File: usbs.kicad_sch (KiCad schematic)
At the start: 34 parts, among them J2 USB-A_Amphenol_UE27AC54100, J3 USB-C_GCT_USB4105-GF-A, J4 USB-C_GCT_USB4105-GF-A, U3 FT4232H_VQFN, Y1 Resonator_12MHz_ABM8G

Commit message: [#93514] Add separating lines, clean schematics
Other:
- moved on the sheet: D6, J3, R30, R31

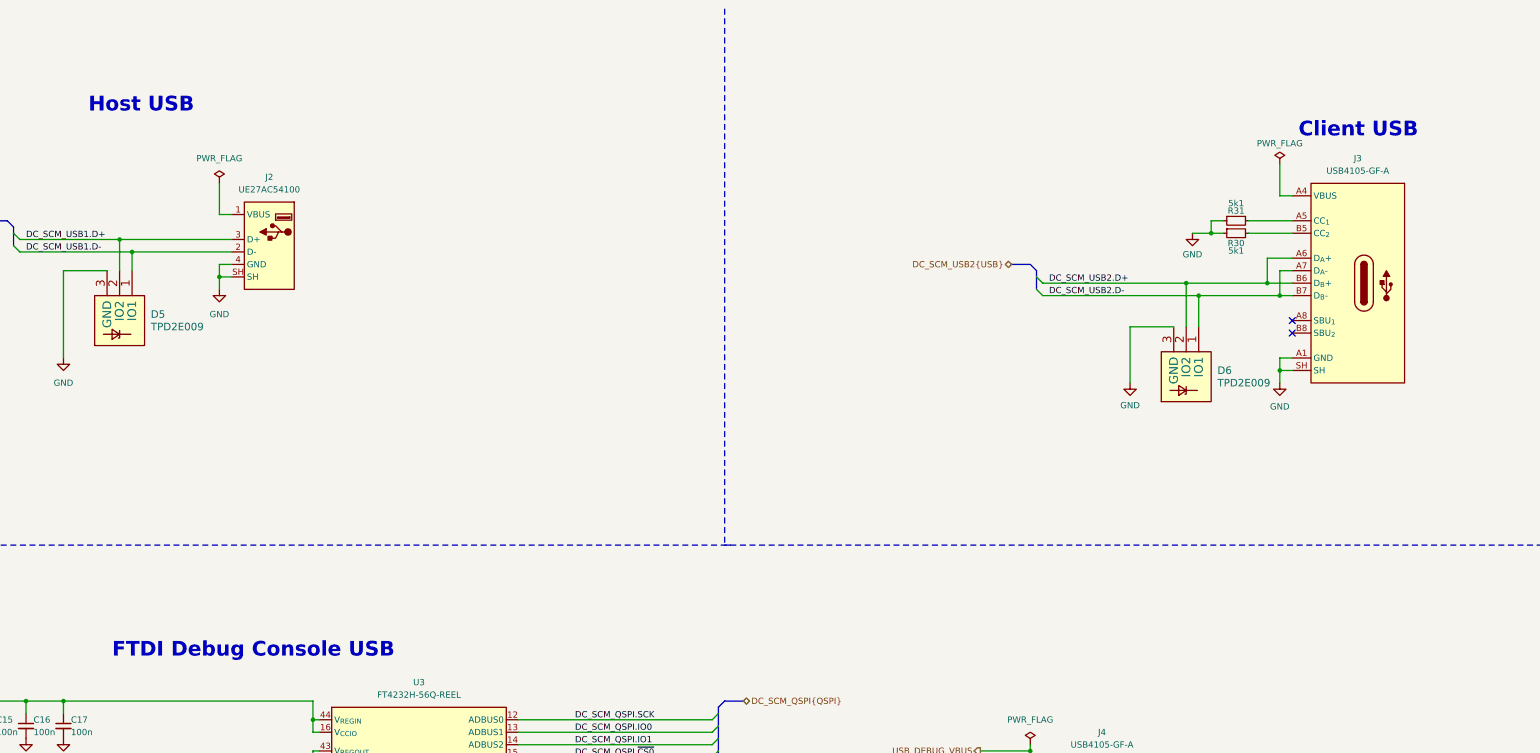
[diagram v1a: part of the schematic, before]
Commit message: [#93514] Align items to grid, add NC-SI testpads
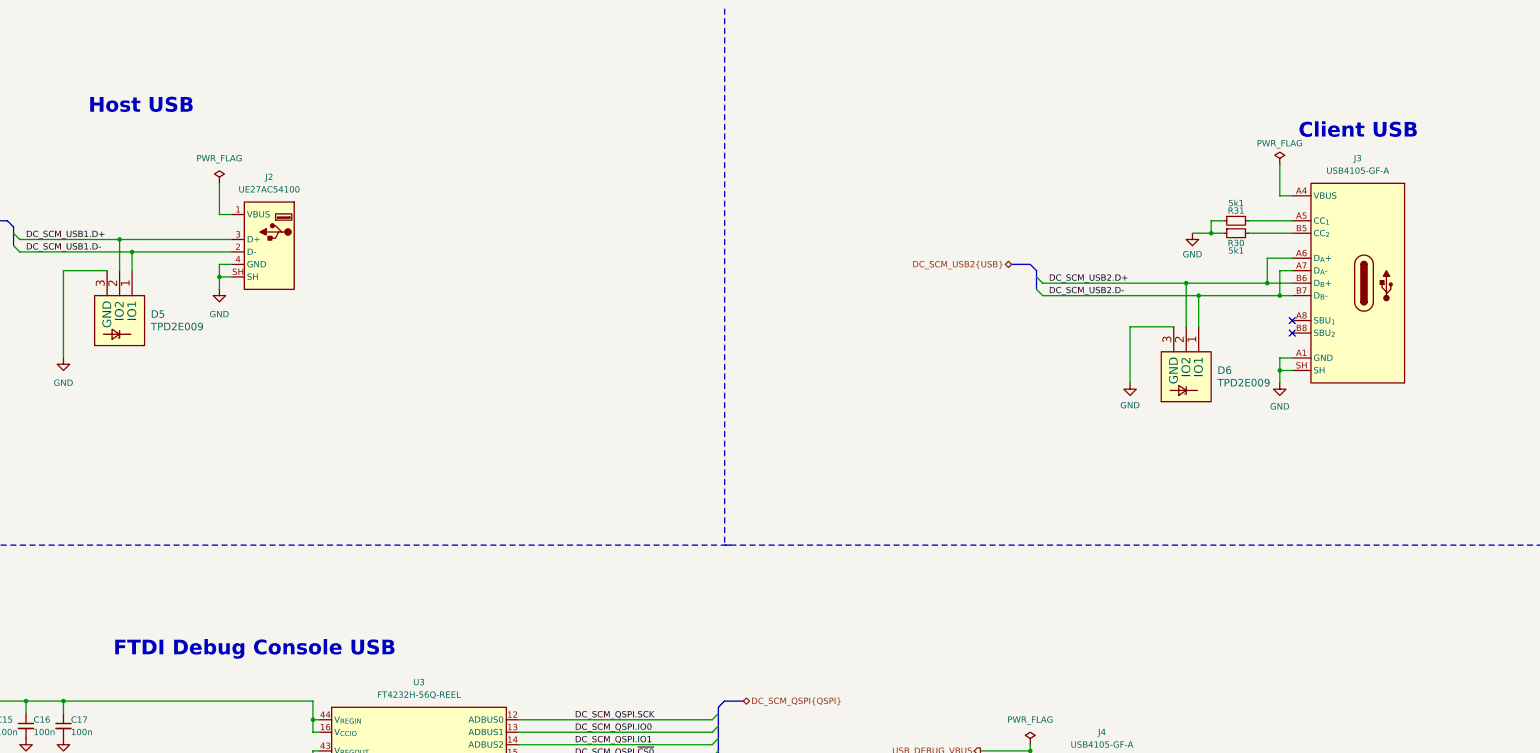
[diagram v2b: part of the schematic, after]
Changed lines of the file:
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@@
 	(text "FTDI Debug Console USB"
 		(exclude_from_sim no)
-		(at 82.296 145.034 0)
+		(at 82.55 144.78 0)
 		(effects
 			(font
@@
 	(text "Host USB"
 		(exclude_from_sim no)
-		(at 77.47 34.036 0)
+		(at 77.47 34.29 0)
 		(effects
 			(font
@@
 	(text "Client USB"
 		(exclude_from_sim no)
-		(at 323.85 39.116 0)
+		(at 323.85 39.37 0)
 		(effects
 			(font

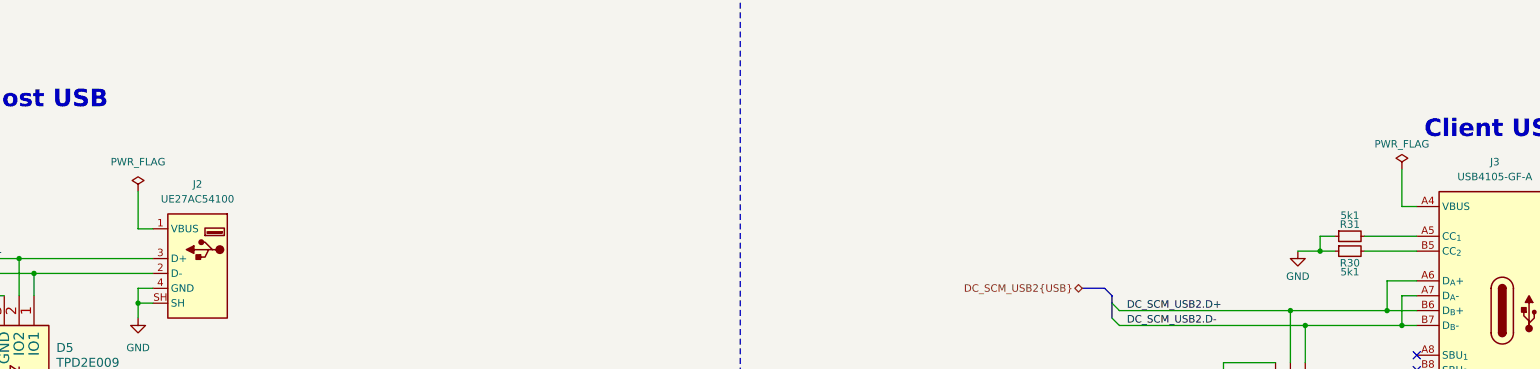
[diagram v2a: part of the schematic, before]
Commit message: [#93514] Add no connect to Host/Client USB VBUS
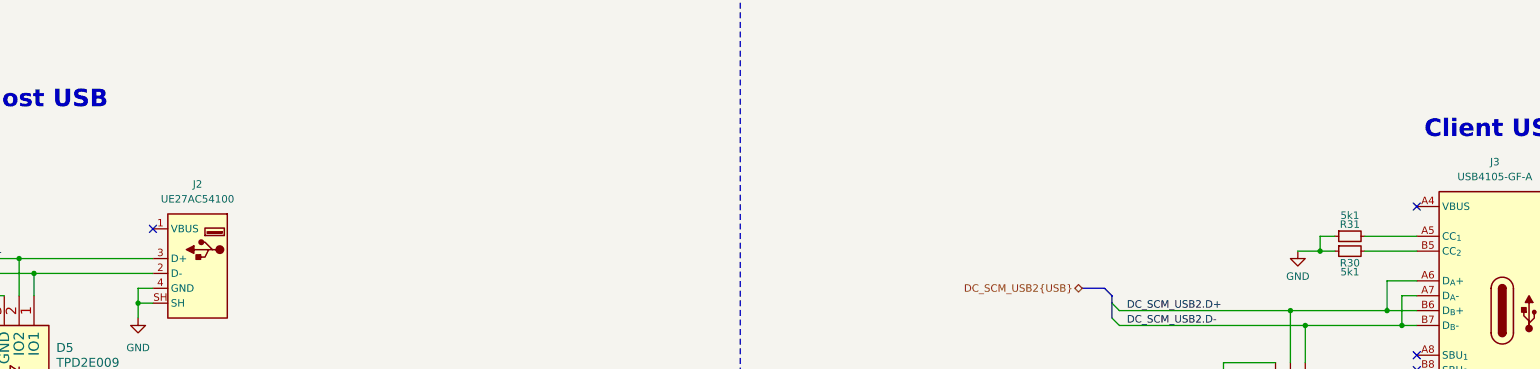
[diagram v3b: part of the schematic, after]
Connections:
- no-connect marks 32 -> 34
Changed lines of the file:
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@@
 	)
 	(no_connect
+		(at 322.58 50.8)
+	)
+	(no_connect
+		(at 106.68 54.61)
+	)
+	(no_connect
 		(at 165.1 175.26)
 	)
@@
 	(wire
 		(pts
-			(xy 320.04 50.8) (xy 322.58 50.8)
-		)
-		(stroke
-			(width 0)
-			(type default)
-		)
-	)
-	(wire
-		(pts
 			(xy 265.43 185.42) (xy 270.51 185.42)
 		)
@@
 	(wire
 		(pts
-			(xy 104.14 48.26) (xy 104.14 54.61)
-		)
-		(stroke
-			(width 0)
-			(type default)
-		)
-	)
-	(wire
-		(pts
 			(xy 267.97 205.74) (xy 267.97 203.2)
 		)
@@
 	(wire
 		(pts
-			(xy 320.04 44.45) (xy 320.04 50.8)
-		)
-		(stroke
-			(width 0)
-			(type default)
-		)
-	)
-	(wire
-		(pts
 			(xy 83.82 59.69) (xy 106.68 59.69)
 		)
@@
 		)
 	)
-	(wire
-		(pts
-			(xy 104.14 54.61) (xy 106.68 54.61)
-		)
-		(stroke
-			(width 0)
-			(type default)
-		)
-	)
 	(label "XO"
 		(at 115.57 217.17 0)
@@
 	)
 	(symbol
-		(lib_id "antmicropower:PWR_FLAG")
-		(at 104.14 48.26 0)
-		(unit 1)
-		(exclude_from_sim no)
-		(in_bom yes)
-		(on_board yes)
-		(dnp no)
-		(fields_autoplaced yes)
-		(property "Reference" "#FLG06"
-			(at 104.14 46.355 0)
-			(effects
-				(font
-					(size 1.27 1.27)
-				)
-				(hide yes)
-			)
-		)
-		(property "Value" "PWR_FLAG"
-			(at 104.14 43.18 0)
-			(effects
-				(font
-					(size 1.27 1.27)
-				)
-			)
-		)
-		(property "Footprint" ""
-			(at 104.14 48.26 0)
-			(effects
-				(font
-					(size 1.27 1.27)
-				)
-				(hide yes)
-			)
-		)
-		(property "Datasheet" ""
-			(at 104.14 48.26 0)
-			(effects
-				(font
-					(size 1.27 1.27)
-				)
-				(hide yes)
-			)
-		)
-		(property "Description" ""
-			(at 104.14 50.8 0)
-			(effects
-				(font
-					(size 1.27 1.27)
-				)
-				(justify left bottom)
-				(hide yes)
-			)
-		)
-		(pin "1"
-		)
-		(instances
-			(project "bmc-breakout-board"
-				(path "/5d67ef28-5805-4f87-b722-2926dabf7f6e/07ab1158-ddfb-42f0-9fa7-f1beb51ab908"
-					(reference "#FLG06")
-					(unit 1)
-				)
-			)
-		)
-	)
-	(symbol
 		(lib_name "FB_600Z_0.5A_Murata-BLM18AG_0603_1")
 		(lib_id "antmicroFerriteBeadsandChips:FB_600Z_0.5A_Murata-BLM18AG_0603")
@@
 					(unit 1)
 				)
-			)
-		)
-	)
-	(symbol
-		(lib_id "antmicropower:PWR_FLAG")
-		(at 320.04 44.45 0)
-		(unit 1)
-		(exclude_from_sim no)
-		(in_bom yes)
-		(on_board yes)
-		(dnp no)
-		(property "Reference" "#FLG07"
-			(at 320.04 42.545 0)
-			(effects
-				(font
-					(size 1.27 1.27)
-				)
-				(hide yes)
-			)
-		)
-		(property "Value" "PWR_FLAG"
-			(at 320.04 40.132 0)
-			(effects
-				(font
-					(size 1.27 1.27)
-				)
-			)
-		)
-		(property "Footprint" ""
-			(at 320.04 44.45 0)
-			(effects
-				(font
-					(size 1.27 1.27)
-				)
-				(hide yes)
-			)
-		)
-		(property "Datasheet" ""
-			(at 320.04 44.45 0)
-			(effects
-				(font
-					(size 1.27 1.27)
-				)
-				(hide yes)
-			)
-		)
-		(property "Description" ""
-			(at 320.04 46.99 0)
-			(effects
-				(font
-					(size 1.27 1.27)
-				)
-				(justify left bottom)
-				(hide yes)
-			)
-		)
-		(pin "1"
-		)
-		(instances
-			(project "bmc-breakout-board"
-				(path "/5d67ef28-5805-4f87-b722-2926dabf7f6e/07ab1158-ddfb-42f0-9fa7-f1beb51ab908"
-					(reference "#FLG07")
-					(unit 1)
-				)

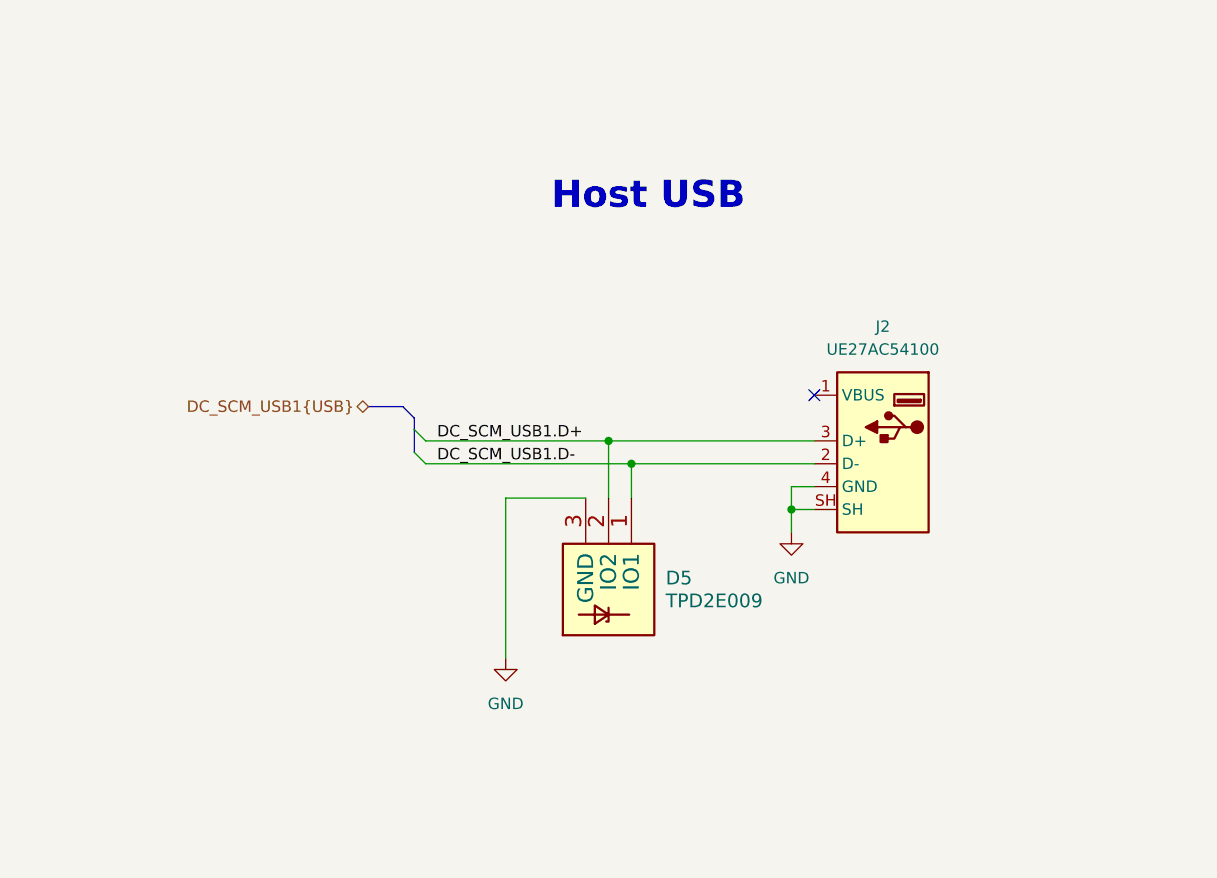
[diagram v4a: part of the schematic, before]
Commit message: [#93949] change USB HOST from USB A to USB C
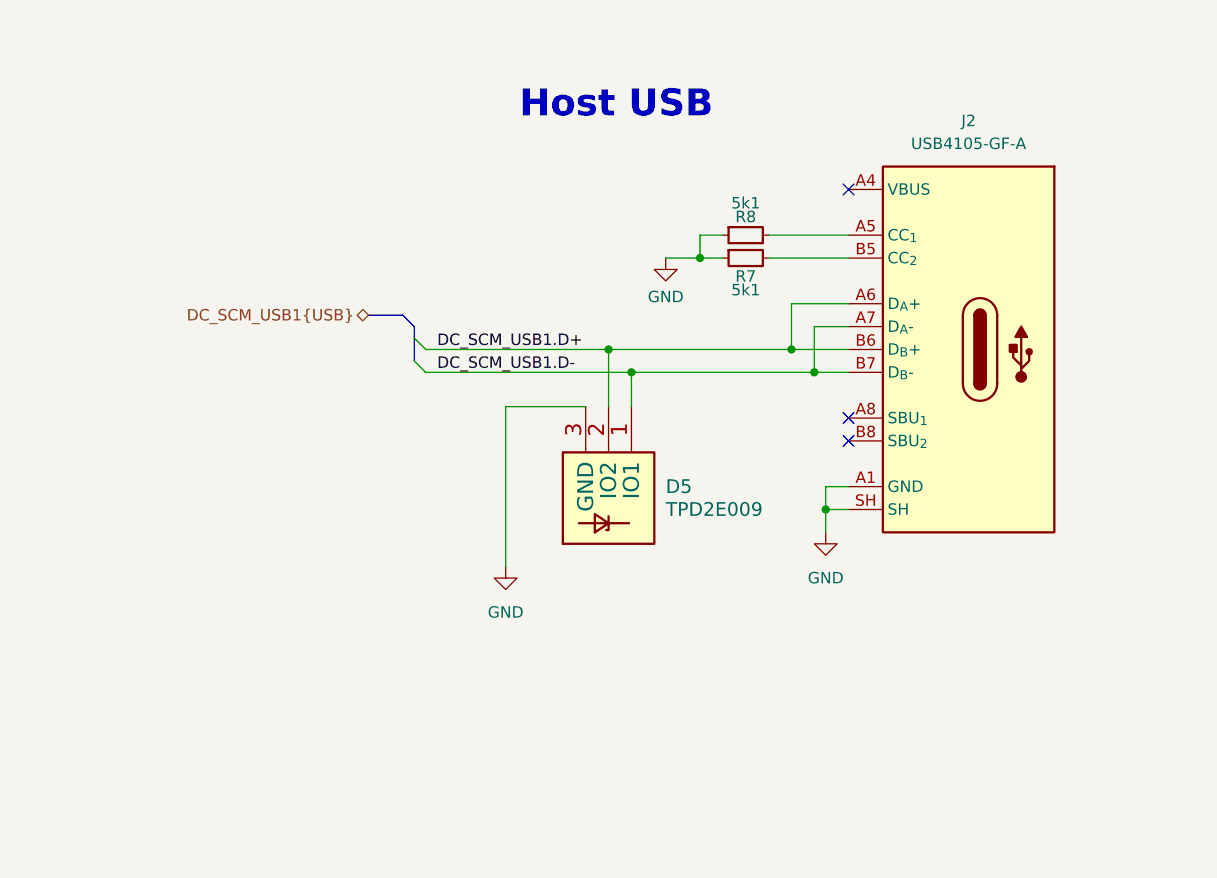
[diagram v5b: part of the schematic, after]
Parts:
- removed J2: USB-A_Amphenol_UE27AC54100, antmicro-footprints:USB-A_Receptacle_Amphenol_UE27AC54100, symbol antmicroUSBConnectors:USB-A_Amphenol_UE27AC54100
- added J2: USB-C_GCT_USB4105-GF-A, antmicro-footprints:USB-C_Receptacle_GCT_USB4105-GF-A, symbol antmicroUSBConnectors:USB-C_GCT_USB4105-GF-A
- added R7, R8: R_5k1_0402, antmicro-footprints:R_0402_1005Metric, symbol antmicroResistors0402:R_5k1_0402
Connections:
- net DC_SCM_USB1.D+: now also J2.A6 (D_{A}+), J2.B6 (D_{B}+)
- net DC_SCM_USB1.D-: now also J2.A7 (D_{A}-), J2.B7 (D_{B}-)
- net GND: now also J2.A1 (GND), J2.A12 (GND), J2.B1 (GND), J2.B12 (GND), J2.SH, R7.1, R8.1
- new net: J2.A5 (CC_{1}), R7.2
- new net: J2.A4 (VBUS), J2.A9 (VBUS), J2.B4 (VBUS), J2.B9 (VBUS)
- new net: J2.B5 (CC_{2}), R8.2
- no-connect marks 34 -> 36
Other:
- moved on the sheet: D5
